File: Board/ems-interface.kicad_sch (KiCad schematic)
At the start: 52 parts, among them J8 EMS, Q11 BC848, Q3 BC848, U2 LM393, U3 MP1584

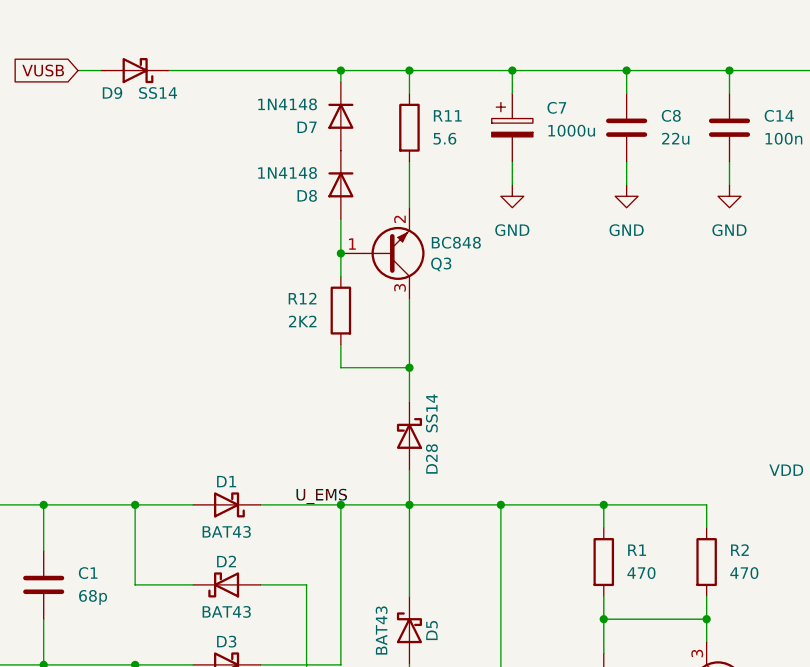
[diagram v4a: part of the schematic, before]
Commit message: Replaces Q3 with higher current type
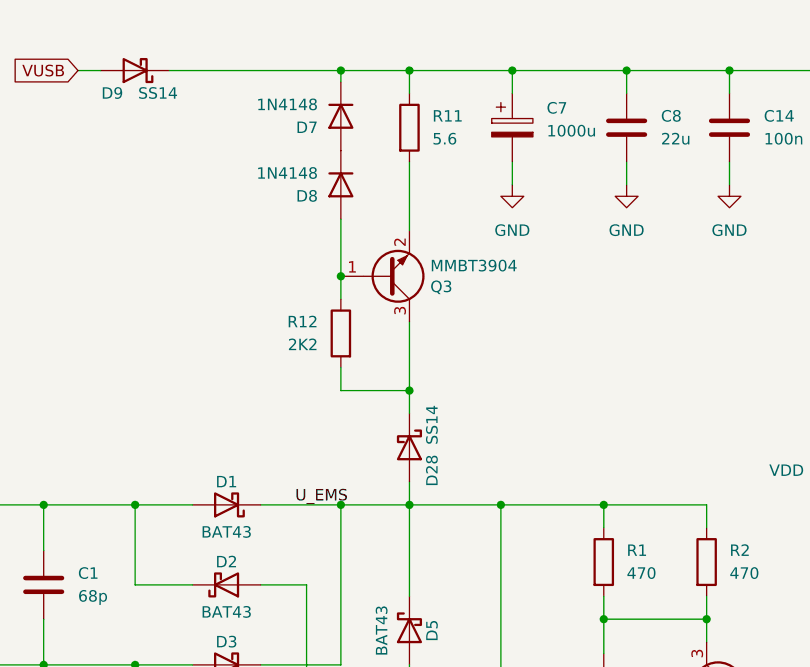
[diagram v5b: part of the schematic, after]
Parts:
- Q3: value BC848 -> MMBT3904
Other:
- moved on the sheet: D28, Q3, R12
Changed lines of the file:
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@@
 	)
 	(junction
+		(at 93.98 88.9)
+		(diameter 0)
+		(color 0 0 0 0)
+	)
+	(junction
 		(at 115.57 101.6)
 		(diameter 0)
@@
 	)
 	(junction
+		(at 86.36 76.2)
+		(diameter 0)
+		(color 0 0 0 0)
+	)
+	(junction
 		(at 198.12 53.34)
 		(diameter 0)
@@
 	)
 	(junction
-		(at 86.36 73.66)
-		(diameter 0)
-		(color 0 0 0 0)
-	)
-	(junction
 		(at 237.49 53.34)
 		(diameter 0)
@@
 	)
 	(junction
-		(at 93.98 86.36)
-		(diameter 0)
-		(color 0 0 0 0)
-	)
-	(junction
 		(at 63.5 119.38)
 		(diameter 0)
@@
 	(wire
 		(pts
-			(xy 86.36 73.66) (xy 86.36 69.85)
-		)
-		(stroke
-			(width 0)
-			(type default)
-		)
-	)
-	(wire
-		(pts
 			(xy 104.14 156.21) (xy 104.14 158.75)
 		)
@@
 	(wire
 		(pts
-			(xy 93.98 78.74) (xy 93.98 86.36)
-		)
-		(stroke
-			(width 0)
-			(type default)
-		)
-	)
-	(wire
-		(pts
 			(xy 237.49 53.34) (xy 233.68 53.34)
 		)
@@
 	(wire
 		(pts
-			(xy 86.36 86.36) (xy 93.98 86.36)
+			(xy 86.36 88.9) (xy 93.98 88.9)
 		)
 		(stroke
@@
 	(wire
 		(pts
+			(xy 93.98 81.28) (xy 93.98 88.9)
+		)
+		(stroke
+			(width 0)
+			(type default)
+		)
+	)
+	(wire
+		(pts
 			(xy 222.25 53.34) (xy 226.06 53.34)
 		)
@@
 	(wire
 		(pts
-			(xy 93.98 97.79) (xy 93.98 101.6)
+			(xy 93.98 99.06) (xy 93.98 101.6)
 		)
 		(stroke
@@
 	(wire
 		(pts
-			(xy 93.98 63.5) (xy 93.98 68.58)
+			(xy 93.98 63.5) (xy 93.98 71.12)
 		)
 		(stroke
@@
 	(wire
 		(pts
-			(xy 86.36 83.82) (xy 86.36 86.36)
+			(xy 86.36 86.36) (xy 86.36 88.9)
 		)
 		(stroke
@@
 	(wire
 		(pts
-			(xy 260.35 57.15) (xy 260.35 53.34)
+			(xy 86.36 76.2) (xy 86.36 78.74)
 		)
 		(stroke
@@
 	(wire
 		(pts
-			(xy 86.36 54.61) (xy 86.36 53.34)
+			(xy 260.35 57.15) (xy 260.35 53.34)
 		)
 		(stroke
@@
 	(wire
 		(pts
-			(xy 180.34 45.72) (xy 180.34 36.83)
+			(xy 86.36 54.61) (xy 86.36 53.34)
 		)
 		(stroke
@@
 	(wire
 		(pts
-			(xy 93.98 53.34) (xy 105.41 53.34)
+			(xy 180.34 45.72) (xy 180.34 36.83)
 		)
 		(stroke
@@
 	(wire
 		(pts
-			(xy 93.98 86.36) (xy 93.98 90.17)
+			(xy 93.98 53.34) (xy 105.41 53.34)
 		)
 		(stroke
@@
 	(wire
 		(pts
-			(xy 86.36 73.66) (xy 86.36 76.2)
+			(xy 170.18 147.32) (xy 170.18 148.59)
 		)
 		(stroke
@@
 	(wire
 		(pts
-			(xy 170.18 147.32) (xy 170.18 148.59)
+			(xy 93.98 88.9) (xy 93.98 91.44)
 		)
 		(stroke
@@
 		)
 	)
+	(wire
+		(pts
+			(xy 86.36 69.85) (xy 86.36 76.2)
+		)
+		(stroke
+			(width 0)
+			(type default)
+		)
+	)
 	(label "EMS_UREF"
 		(at 149.86 176.53 0)
@@
 	(symbol
 		(lib_id "Device:D_Schottky")
-		(at 93.98 93.98 270)
+		(at 93.98 95.25 270)
 		(unit 1)
 		(exclude_from_sim no)
@@
 		(dnp no)
 		(property "Reference" "D28"
-			(at 96.52 96.52 0)
+			(at 96.52 97.79 0)
 			(effects
 				(font
@@
 		)
 		(property "Value" "SS14"
-			(at 96.52 91.44 0)
+			(at 96.52 92.71 0)
 			(effects
 				(font
@@
 		)
 		(property "Footprint" "Diode_SMD:D_SMA"
-			(at 93.98 93.98 0)
+			(at 93.98 95.25 0)
 			(effects
 				(font
@@
 		)
 		(property "Datasheet" "~"
-			(at 93.98 93.98 0)
+			(at 93.98 95.25 0)
 			(effects
 				(font
@@
 		)
 		(property "Description" ""
-			(at 93.98 93.98 0)
+			(at 93.98 95.25 0)
 			(effects
 				(font
@@
 	(symbol
 		(lib_id "Device:R")
-		(at 86.36 80.01 0)
+		(at 86.36 82.55 0)
 		(mirror y)
 		(unit 1)
@@
 		(dnp no)
 		(property "Reference" "R12"
-			(at 83.82 78.7399 0)
+			(at 83.82 81.2799 0)
 			(effects
 				(font
@@
 		)
 		(property "Value" "2K2"
-			(at 83.82 81.2799 0)
+			(at 83.82 83.8199 0)
 			(effects
 				(font
@@
 		)
 		(property "Footprint" "Resistor_SMD:R_0805_2012Metric"
-			(at 88.138 80.01 90)
+			(at 88.138 82.55 90)
 			(effects
 				(font
@@
 		)
 		(property "Datasheet" "~"
-			(at 86.36 80.01 0)
+			(at 86.36 82.55 0)
 			(effects
 				(font
@@
 		)
 		(property "Description" "Resistor"
-			(at 86.36 80.01 0)
+			(at 86.36 82.55 0)
 			(effects
 				(font
@@
 	(symbol
 		(lib_id "Transistor_BJT:BC850")
-		(at 91.44 73.66 0)
+		(at 91.44 76.2 0)
 		(mirror x)
 		(unit 1)
@@
 		(dnp no)
 		(property "Reference" "Q3"
-			(at 96.2914 74.8284 0)
+			(at 96.2914 77.3684 0)
 			(effects
 				(font
@@
 			)
 		)
-		(property "Value" "BC848"
-			(at 96.2914 72.517 0)
+		(property "Value" "MMBT3904"
+			(at 96.2914 75.057 0)
 			(effects
 				(font
@@
 		)
 		(property "Footprint" "Package_TO_SOT_SMD:SOT-23"
-			(at 96.52 71.755 0)
+			(at 96.52 74.295 0)
 			(effects
 				(font
@@
 		)
 		(property "Datasheet" "http://www.infineon.com/dgdl/Infineon-BC847SERIES_BC848SERIES_BC849SERIES_BC850SERIES-DS-v01_01-en.pdf?fileId=db3a304314dca389011541d4630a1657"
-			(at 91.44 73.66 0)
+			(at 91.44 76.2 0)
 			(effects
 				(font
@@
 		)
 		(property "Description" "0.1A Ic, 45V Vce, NPN Transistor, SOT-23"
-			(at 91.44 73.66 0)
+			(at 91.44 76.2 0)
 			(effects
 				(font
